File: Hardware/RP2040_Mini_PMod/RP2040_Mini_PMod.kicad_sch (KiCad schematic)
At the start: 41 parts, among them J1 Micro_SD_Card, J3 Conn_02x06_Odd_Even, J4 USB_C_Receptacle_USB2.0, SW1 PTS815 SJK 250 SMTR LFS, SW2 PTS815 SJK 250 SMTR LFS, U1 RP2040, U2 W25Q128JVS, U3 NCP1117-3.3_SOT223, Y1 12MHz

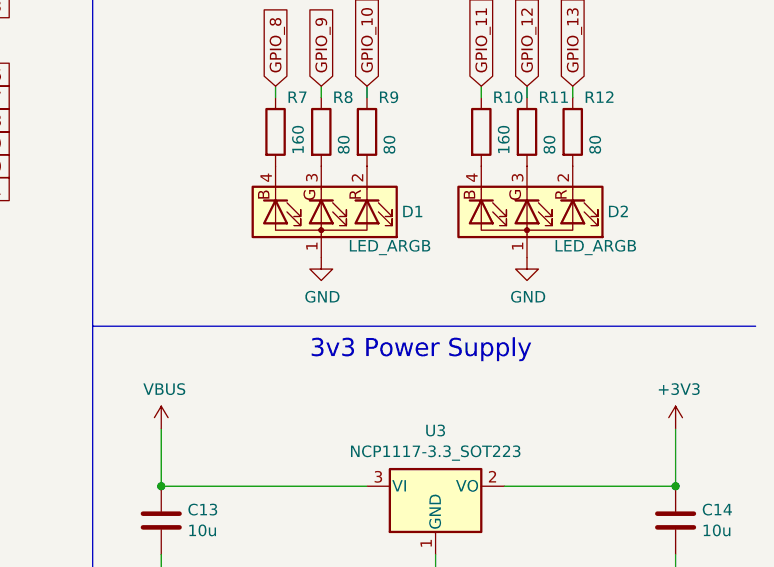
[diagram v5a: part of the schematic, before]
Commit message: correct 3v3 issue for #31 with LED's
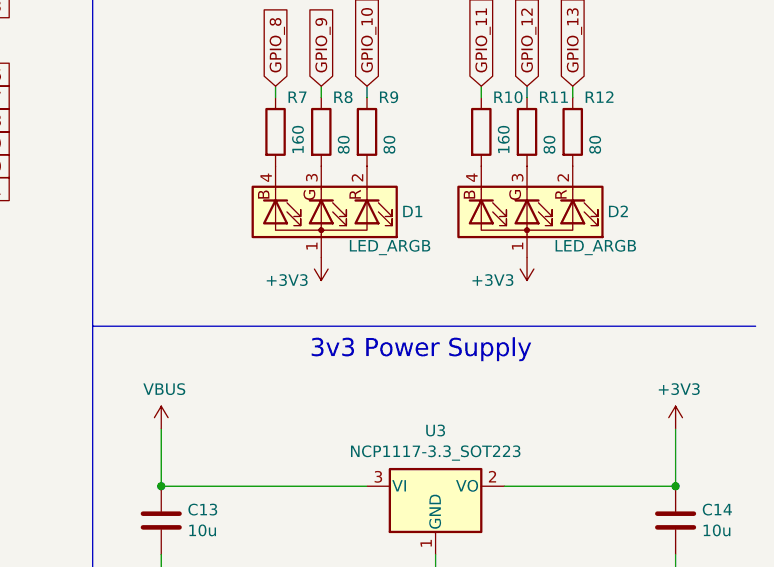
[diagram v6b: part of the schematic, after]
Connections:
- net +3V3: now also D1.1 (A), D2.1 (A)
- net GND: no longer D1.1 (A), D2.1 (A)
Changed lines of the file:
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@@
     (pin "2")
-  )
-  (symbol (lib_id "power:GND") (at 259.08 121.92 0) (unit 1)
-    (in_bom yes) (on_board yes)
-    (property "Reference" "#PWR0105" (id 0) (at 259.08 128.27 0)
-      (effects (font (size 1.27 1.27)) hide)
-    )
-    (property "Value" "GND" (id 1) (at 259.207 126.3142 0))
-    (property "Footprint" "" (id 2) (at 259.08 121.92 0)
-      (effects (font (size 1.27 1.27)) hide)
-    )
-    (property "Datasheet" "" (id 3) (at 259.08 121.92 0)
-      (effects (font (size 1.27 1.27)) hide)
-    )
-    (pin "1")
   )
   (symbol (lib_id "Switch:SW_MEC_5E") (at 100.33 187.96 90) (unit 1)
@@
     (pin "4")
   )
+  (symbol (lib_id "power:+3V3") (at 236.22 121.92 180) (unit 1)
+    (in_bom yes) (on_board yes)
+    (property "Reference" "#PWR?" (id 0) (at 236.22 118.11 0)
+      (effects (font (size 1.27 1.27)) hide)
+    )
+    (property "Value" "+3V3" (id 1) (at 232.41 124.46 0))
+    (property "Footprint" "" (id 2) (at 236.22 121.92 0)
+      (effects (font (size 1.27 1.27)) hide)
+    )
+    (property "Datasheet" "" (id 3) (at 236.22 121.92 0)
+      (effects (font (size 1.27 1.27)) hide)
+    )
+    (pin "1")
+  )
   (symbol (lib_id "power:+3V3") (at 223.52 67.31 90) (unit 1)
     (in_bom yes) (on_board yes)
@@
     (pin "2")
   )
+  (symbol (lib_id "power:+3V3") (at 259.08 121.92 180) (unit 1)
+    (in_bom yes) (on_board yes)
+    (property "Reference" "#PWR?" (id 0) (at 259.08 118.11 0)
+      (effects (font (size 1.27 1.27)) hide)
+    )
+    (property "Value" "+3V3" (id 1) (at 255.27 124.46 0))
+    (property "Footprint" "" (id 2) (at 259.08 121.92 0)
+      (effects (font (size 1.27 1.27)) hide)
+    )
+    (property "Datasheet" "" (id 3) (at 259.08 121.92 0)
+      (effects (font (size 1.27 1.27)) hide)
+    )
+    (pin "1")
+  )
   (symbol (lib_id "Connector:TestPoint") (at 46.99 38.1 270) (unit 1)
     (in_bom yes) (on_board yes) (fields_autoplaced)
@@
     (pin "1")
     (pin "2")
-  )
-  (symbol (lib_id "power:GND") (at 236.22 121.92 0) (unit 1)
-    (in_bom yes) (on_board yes)
-    (property "Reference" "#PWR0106" (id 0) (at 236.22 128.27 0)
-      (effects (font (size 1.27 1.27)) hide)
-    )
-    (property "Value" "GND" (id 1) (at 236.347 126.3142 0))
-    (property "Footprint" "" (id 2) (at 236.22 121.92 0)
-      (effects (font (size 1.27 1.27)) hide)
-    )
-    (property "Datasheet" "" (id 3) (at 236.22 121.92 0)
-      (effects (font (size 1.27 1.27)) hide)
-    )
-    (pin "1")
   )
   (symbol (lib_name "GND_1") (lib_id "power:GND") (at 223.52 72.39 270) (unit 1)
@@
       (reference "#PWR0104") (unit 1) (value "GND") (footprint "")
     )
-    (path "/83da84e2-a2de-4340-b9b8-756fed6db649"
-      (reference "#PWR0105") (unit 1) (value "GND") (footprint "")
-    )
-    (path "/c69faba3-3eb3-4244-a003-fbe4a304627f"
-      (reference "#PWR0106") (unit 1) (value "GND") (footprint "")
-    )
     (path "/ccfe8d2f-71d5-404f-9b96-514112dd35a5"
       (reference "#PWR0107") (unit 1) (value "GND") (footprint "")
@@
       (reference "#PWR0150") (unit 1) (value "GND") (footprint "")
     )
+    (path "/9bad22a9-9560-430b-b24c-45d329d79933"
+      (reference "#PWR?") (unit 1) (value "+3V3") (footprint "")
+    )
+    (path "/adba15d5-8fd9-4ab6-8821-f5577dd3d6d7"
+      (reference "#PWR?") (unit 1) (value "+3V3") (footprint "")
+    )
     (path "/00000000-0000-0000-0000-000060f5155c"

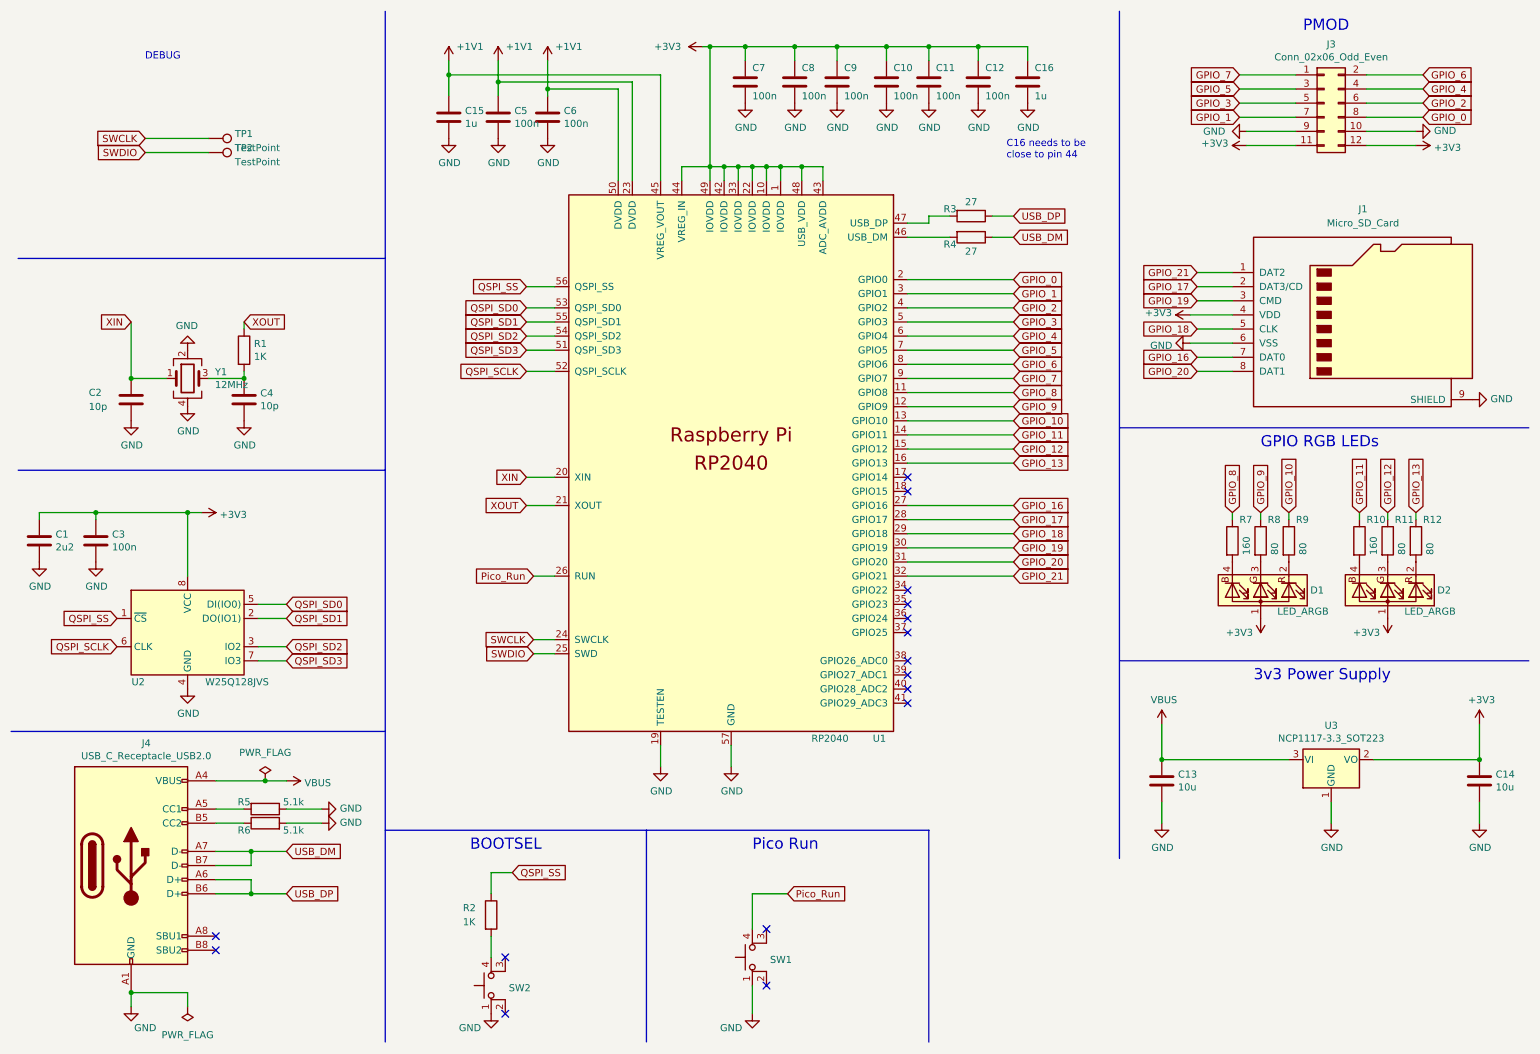
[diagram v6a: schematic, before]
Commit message: upgrade to kicad 7.0
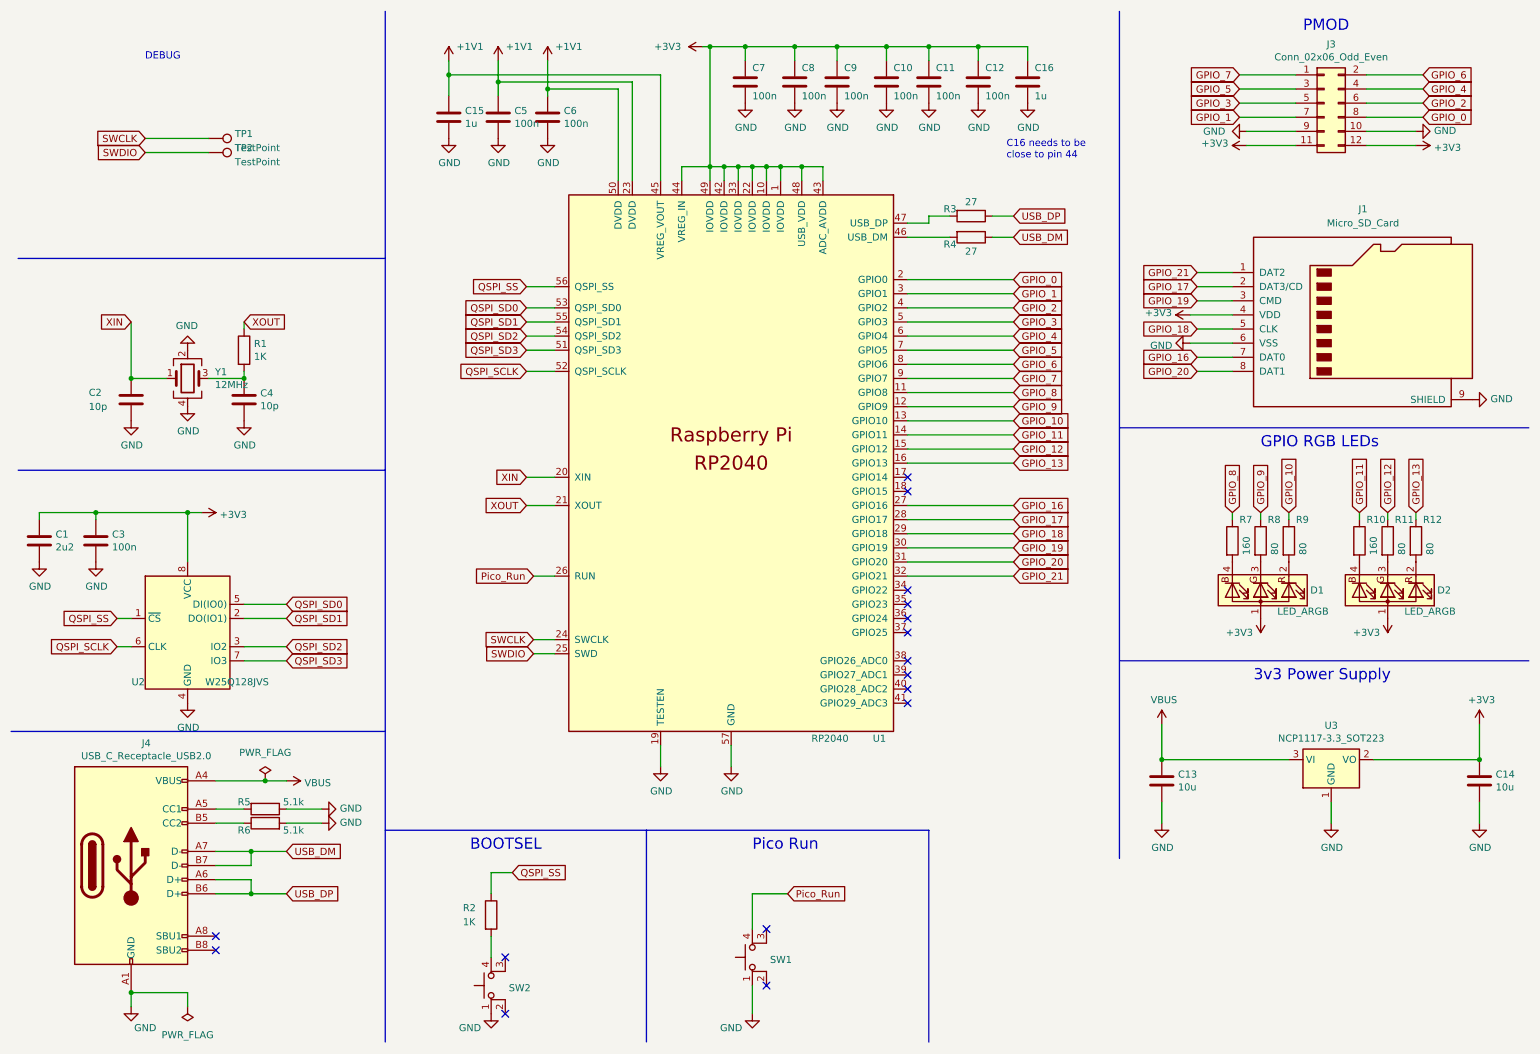
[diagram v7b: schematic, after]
